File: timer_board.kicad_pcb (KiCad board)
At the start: 2 copper layers, 101.6 x 76.2 mm, 52 parts, among them IC1 ATMEGA32U4, P1 USBMICRO, P2 OUT_INV, P3 Trigger, P4 OUT, Q1 NPN, Q2 NPN, U1 DS3231N, U2 74HC04, Y1 RESONATORSMD

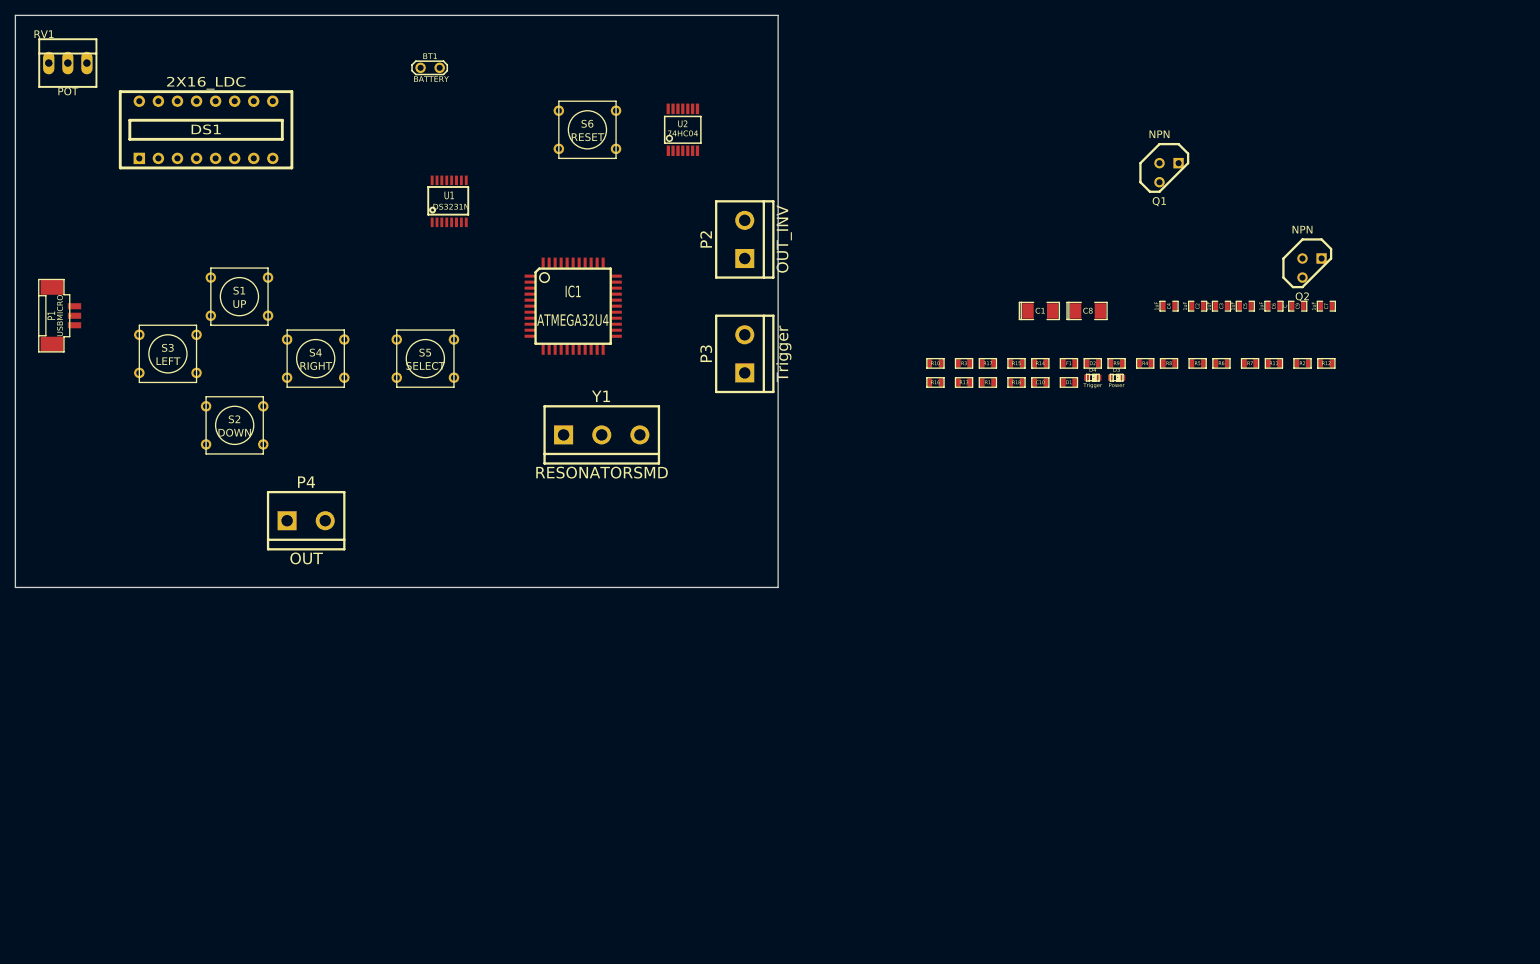
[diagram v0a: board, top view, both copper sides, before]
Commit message: Added LCD and USB Micro
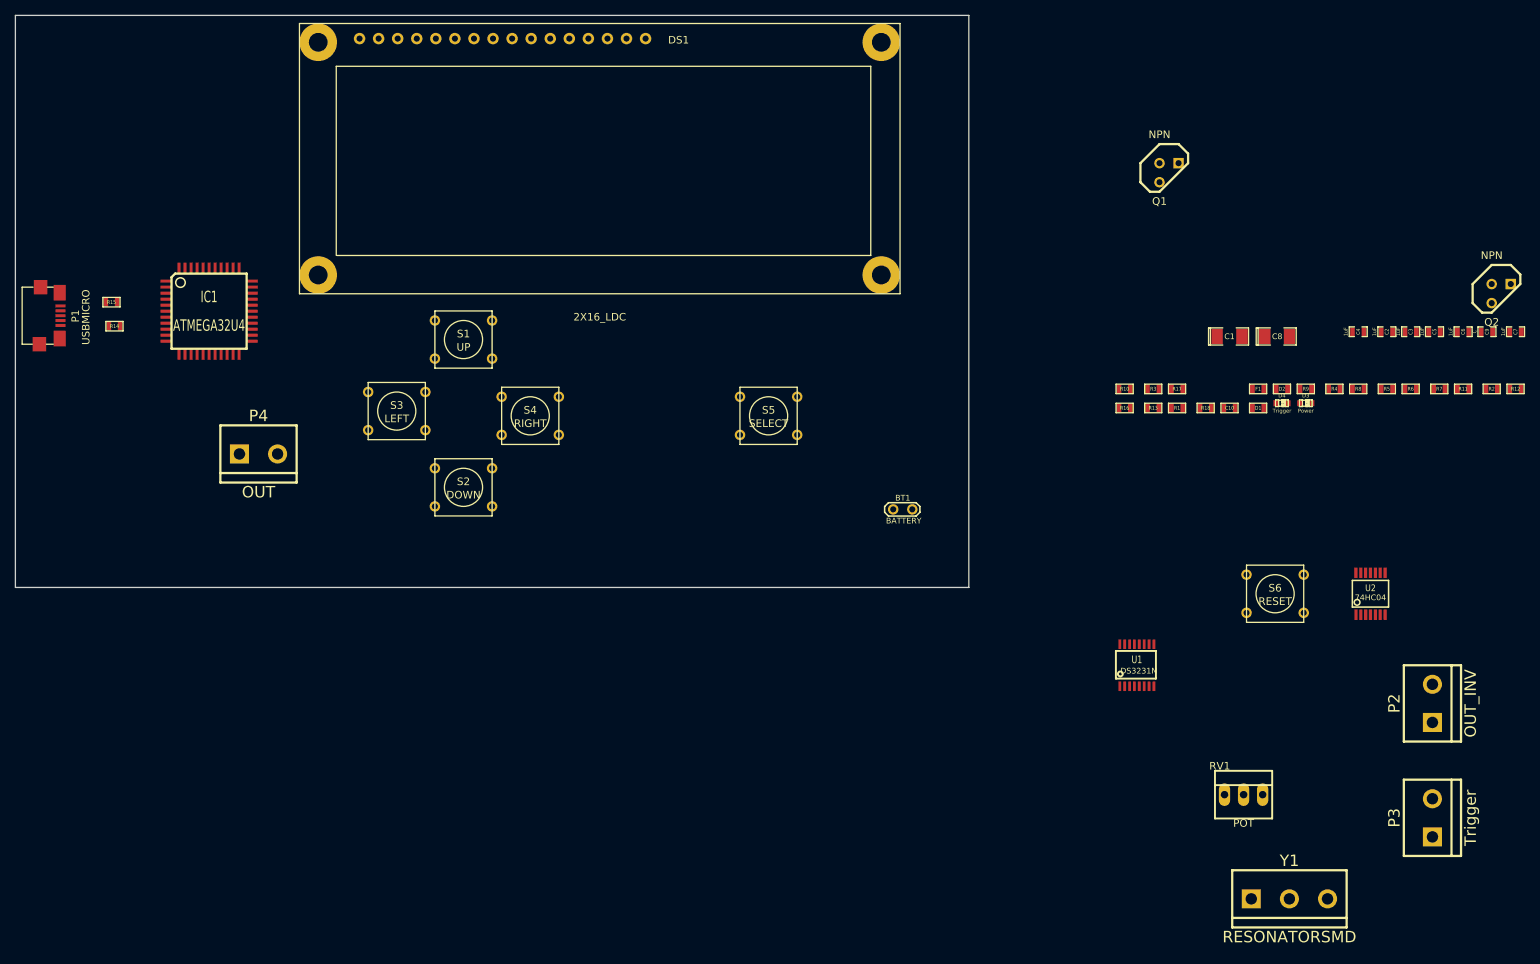
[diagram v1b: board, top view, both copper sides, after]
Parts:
- DS1: footprint SWDIP8 -> LCD16X2
- P1: footprint CONN3-INV_SMD -> USB-MICRO-B
- moved RV1 184.5 mm to (189.0, 129.2)
- moved R14 123.4 mm to (38.6, 66.8)
- moved R15 120.8 mm to (38.2, 63.6)
- moved U2 110.5 mm to (205.9, 102.4)
- moved Y1 110.5 mm to (195.1, 143.1)
- moved P2 110.5 mm to (214.2, 117.0)
- moved P3 110.5 mm to (214.2, 132.3)
- moved S6 110.5 mm to (193.2, 102.4)
- moved U1 110.5 mm to (174.8, 112.0)
- moved BT1 86.2 mm to (143.6, 91.2)
- moved IC1 48.5 mm to (51.2, 64.8)
- moved S5 46.4 mm to (125.7, 78.7)
- moved S2 31.6 mm to (85.1, 88.3)
- moved S3 31.4 mm to (76.2, 78.1)
- moved S1 30.4 mm to (85.1, 68.6)
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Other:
- board size 101.6 x 76.2 mm -> 127 x 76.2 mm

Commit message: moved a few things arround
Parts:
- moved Q2 107.3 mm to (116.2, 68.6)
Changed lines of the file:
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@@
   )
   (module TO92 (layer F.Cu)
-    (at 223.32 62.455)
+    (at 116.205 68.58)
     (descr "Transistor TO92 brochage type BC237")
     (tags "TR TO92")
